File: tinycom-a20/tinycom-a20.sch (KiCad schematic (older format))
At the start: 38 parts, among them P1 CONN_02X08, P2 CONN_02X08, U1 ALLWINNERA10/TFBGA441, U2 H5TQG63BFR/FBGA96, U3 H27UBG8T2A/TSOP48, U4 H5TQG63BFR/FBGA96, Y1 Crystal_Small, Y2 Crystal_Small

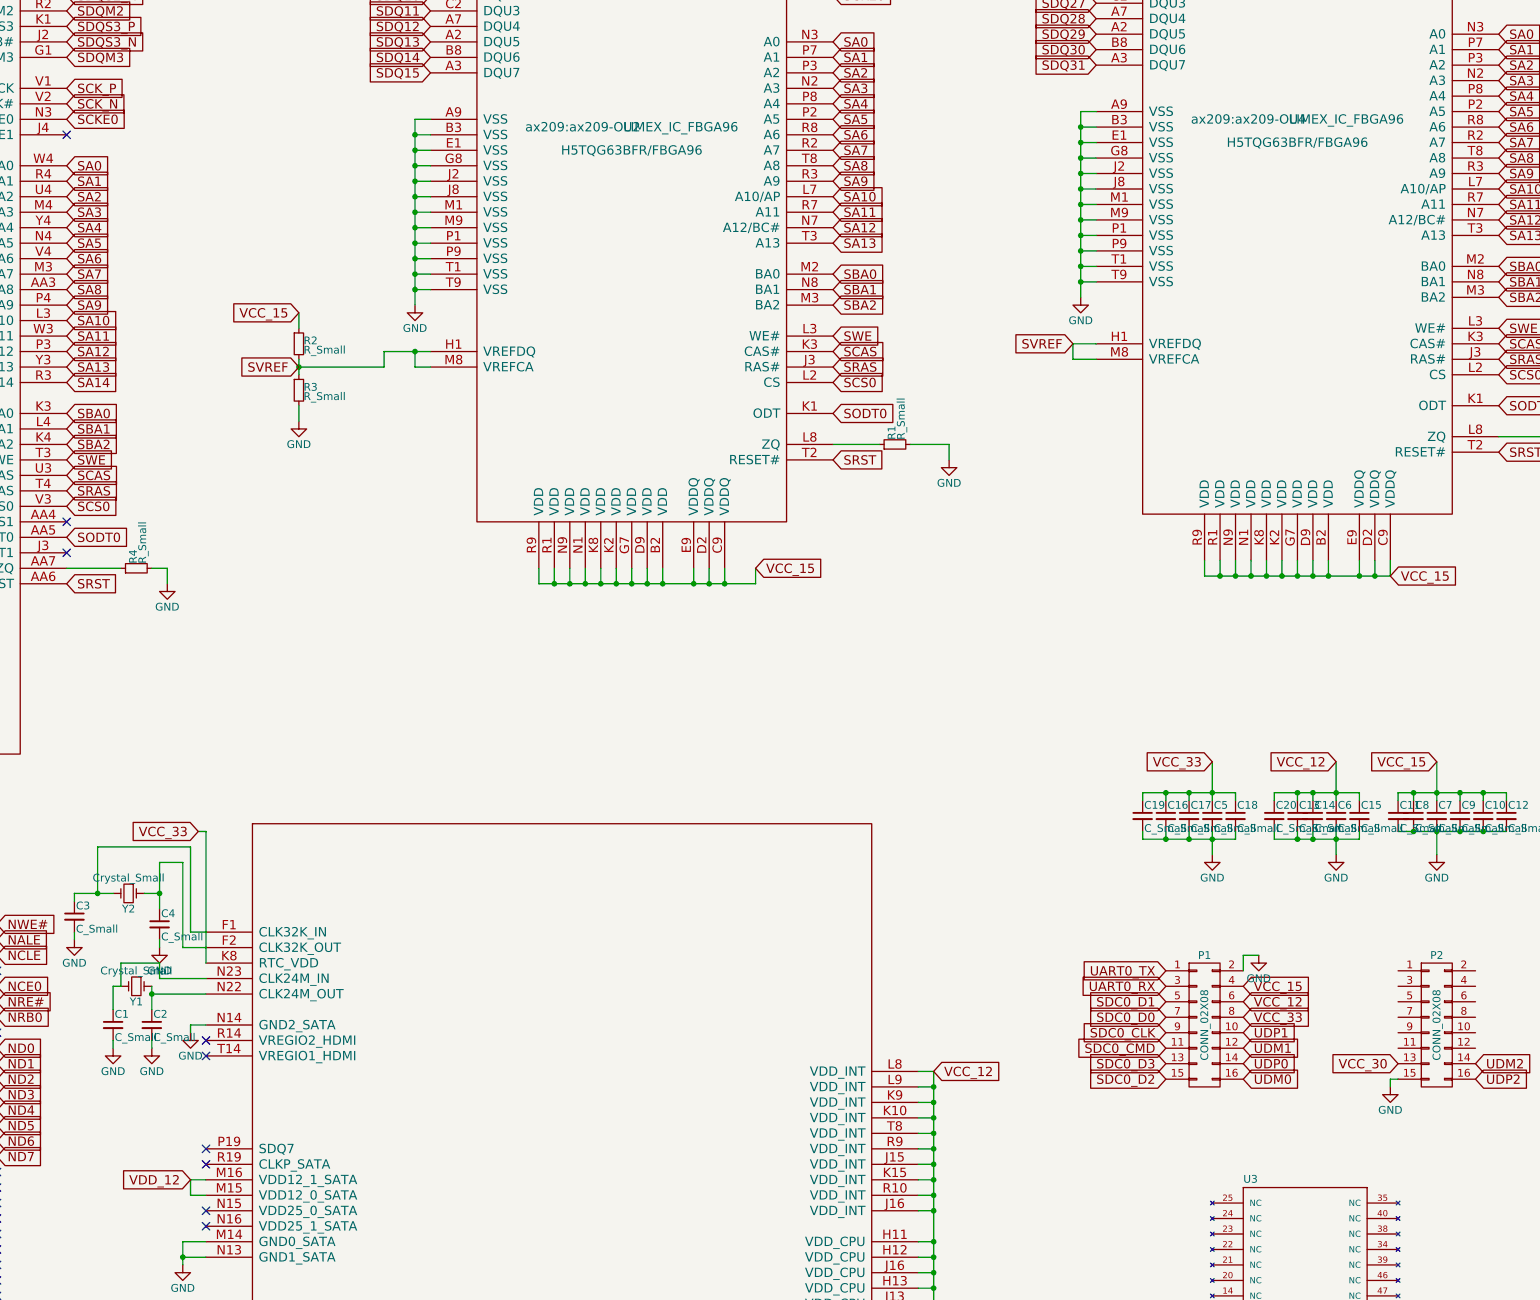
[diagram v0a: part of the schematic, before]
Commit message: change track/via size settings, update ddr footprints
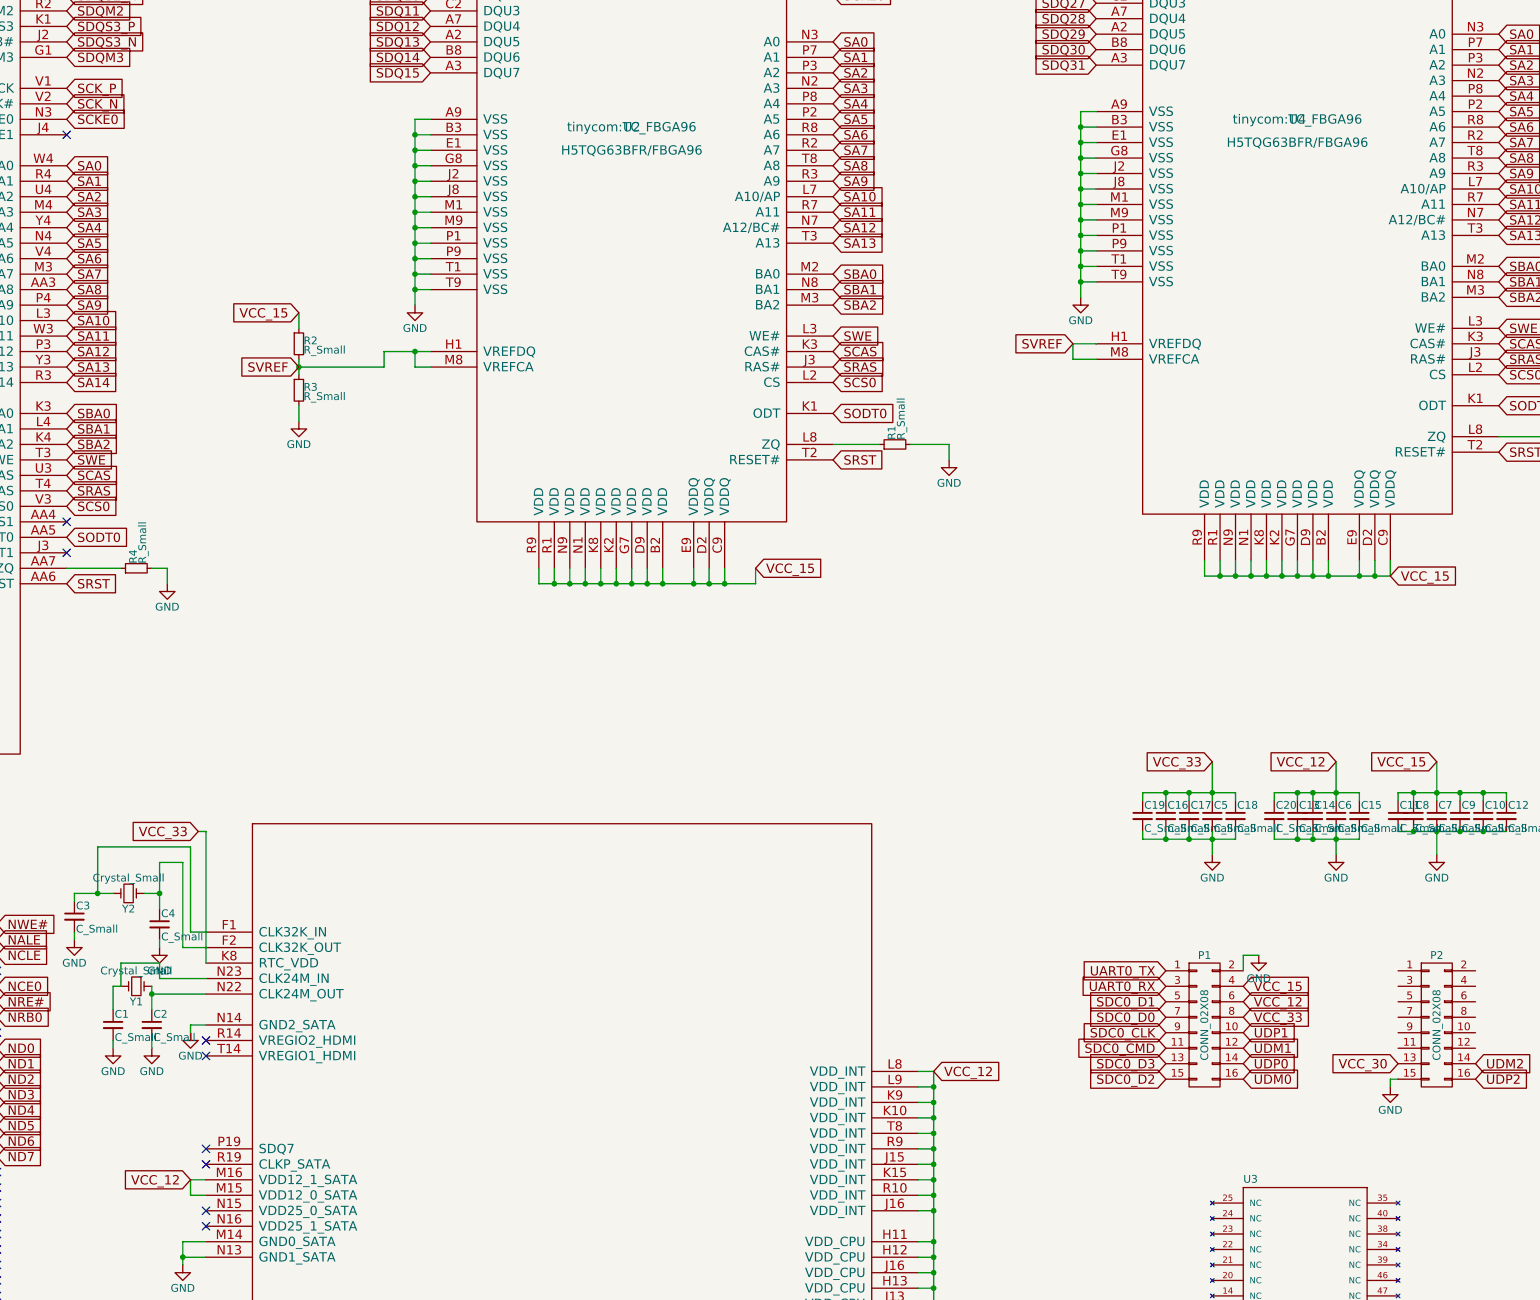
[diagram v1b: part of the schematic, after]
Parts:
- U2, U4: footprint ax209:ax209-OLIMEX_IC_FBGA96 -> tinycom:TC_FBGA96
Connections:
- net VDD_12 is gone; now on net VCC_12: U1.M15 (VDD12_0_SATA), U1.M16 (VDD12_1_SATA)
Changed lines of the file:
@@
 $EndComp
 $Comp
-L GND #PWR21
+L GND #PWR01
 U 1 1 563E445F
 P 17800 6150
-F 0 "#PWR21" H 17800 5900 50  0001 C CNN
+F 0 "#PWR01" H 17800 5900 50  0001 C CNN
 F 1 "GND" H 17800 6000 50  0000 C CNN
 F 2 "" H 17800 6150 60  0000 C CNN
@@
 F 0 "U2" H 15750 4000 60  0000 C CNN
 F 1 "H5TQG63BFR/FBGA96" H 15750 3850 60  0000 C CNN
-F 2 "ax209:ax209-OLIMEX_IC_FBGA96" H 15750 4000 60  0000 C CNN
+F 2 "tinycom:TC_FBGA96" H 15750 4000 60  0000 C CNN
 F 3 "" H 15750 4000 60  0000 C CNN
 	1    15750 4000
@@
 SCK_P
 $Comp
-L GND #PWR19
+L GND #PWR02
 U 1 1 563ECE56
 P 14950 850
-F 0 "#PWR19" H 14950 600 50  0001 C CNN
+F 0 "#PWR02" H 14950 600 50  0001 C CNN
 F 1 "GND" H 14950 700 50  0000 C CNN
 F 2 "" H 14950 850 60  0000 C CNN
@@
 $EndComp
 $Comp
-L GND #PWR17
+L GND #PWR03
 U 1 1 563EDF36
 P 13600 5900
-F 0 "#PWR17" H 13600 5650 50  0001 C CNN
+F 0 "#PWR03" H 13600 5650 50  0001 C CNN
 F 1 "GND" H 13600 5750 50  0000 C CNN
 F 2 "" H 13600 5900 60  0000 C CNN
@@
 $EndComp
 $Comp
-L GND #PWR18
+L GND #PWR04
 U 1 1 563EE398
 P 14350 5150
-F 0 "#PWR18" H 14350 4900 50  0001 C CNN
+F 0 "#PWR04" H 14350 4900 50  0001 C CNN
 F 1 "GND" H 14350 5000 50  0000 C CNN
 F 2 "" H 14350 5150 60  0000 C CNN
@@
 $EndComp
 $Comp
-L GND #PWR10
+L GND #PWR05
 U 1 1 56400687
 P 12400 9950
-F 0 "#PWR10" H 12400 9700 50  0001 C CNN
+F 0 "#PWR05" H 12400 9700 50  0001 C CNN
 F 1 "GND" H 12400 9800 50  0000 C CNN
 F 2 "" H 12400 9950 60  0000 C CNN
@@
 $EndComp
 $Comp
-L GND #PWR11
+L GND #PWR06
 U 1 1 56400704
 P 12650 9950
-F 0 "#PWR11" H 12650 9700 50  0001 C CNN
+F 0 "#PWR06" H 12650 9700 50  0001 C CNN
 F 1 "GND" H 12650 9800 50  0000 C CNN
 F 2 "" H 12650 9950 60  0000 C CNN
@@
 $EndComp
 $Comp
-L GND #PWR9
+L GND #PWR07
 U 1 1 56408532
 P 12150 9250
-F 0 "#PWR9" H 12150 9000 50  0001 C CNN
+F 0 "#PWR07" H 12150 9000 50  0001 C CNN
 F 1 "GND" H 12150 9100 50  0000 C CNN
 F 2 "" H 12150 9250 60  0000 C CNN
@@
 $EndComp
 $Comp
-L GND #PWR12
+L GND #PWR08
 U 1 1 56408573
 P 12700 9300
-F 0 "#PWR12" H 12700 9050 50  0001 C CNN
+F 0 "#PWR08" H 12700 9050 50  0001 C CNN
 F 1 "GND" H 12700 9150 50  0000 C CNN
 F 2 "" H 12700 9300 60  0000 C CNN
@@
 $EndComp
 $Comp
-L GND #PWR14
+L GND #PWR09
 U 1 1 5640D8CA
 P 12750 6950
-F 0 "#PWR14" H 12750 6700 50  0001 C CNN
+F 0 "#PWR09" H 12750 6700 50  0001 C CNN
 F 1 "GND" H 12750 6800 50  0000 C CNN
 F 2 "" H 12750 6950 60  0000 C CNN
@@
 $EndComp
 $Comp
-L GND #PWR26
+L GND #PWR010
 U 1 1 56408FCA
 P 19800 9350
-F 0 "#PWR26" H 19800 9100 50  0001 C CNN
+F 0 "#PWR010" H 19800 9100 50  0001 C CNN
 F 1 "GND" H 19800 9200 50  0000 C CNN
 F 2 "" H 19800 9350 60  0000 C CNN
@@
 UDP2
 $Comp
-L GND #PWR28
+L GND #PWR011
 U 1 1 56411561
 P 20650 10200
-F 0 "#PWR28" H 20650 9950 50  0001 C CNN
+F 0 "#PWR011" H 20650 9950 50  0001 C CNN
 F 1 "GND" H 20650 10050 50  0000 C CNN
 F 2 "" H 20650 10200 60  0000 C CNN
@@
 NoConn ~ 7500 2750
 $Comp
-L GND #PWR8
+L GND #PWR012
 U 1 1 56414A5D
 P 8850 1300
-F 0 "#PWR8" H 8850 1050 50  0001 C CNN
+F 0 "#PWR012" H 8850 1050 50  0001 C CNN
 F 1 "GND" H 8850 1150 50  0000 C CNN
 F 2 "" H 8850 1300 60  0000 C CNN
@@
 VCC_15
 $Comp
-L GND #PWR1
+L GND #PWR013
 U 1 1 56417328
 P 800 9350
-F 0 "#PWR1" H 800 9100 50  0001 C CNN
+F 0 "#PWR013" H 800 9100 50  0001 C CNN
 F 1 "GND" H 800 9200 50  0000 C CNN
 F 2 "" H 800 9350 60  0000 C CNN
@@
 NoConn ~ 1050 13300
 $Comp
-L GND #PWR3
+L GND #PWR014
 U 1 1 56417B02
 P 900 13450
-F 0 "#PWR3" H 900 13200 50  0001 C CNN
+F 0 "#PWR014" H 900 13200 50  0001 C CNN
 F 1 "GND" H 900 13300 50  0000 C CNN
 F 2 "" H 900 13450 60  0000 C CNN
@@
 NoConn ~ 1050 13700
 $Comp
-L GND #PWR2
+L GND #PWR015
 U 1 1 56417F5A
 P 850 13800
-F 0 "#PWR2" H 850 13550 50  0001 C CNN
+F 0 "#PWR015" H 850 13550 50  0001 C CNN
 F 1 "GND" H 850 13650 50  0000 C CNN
 F 2 "" H 850 13800 60  0000 C CNN
@@
 NoConn ~ 5650 11400
 $Comp
-L GND #PWR6
+L GND #PWR016
 U 1 1 56418E41
 P 5850 12050
-F 0 "#PWR6" H 5850 11800 50  0001 C CNN
+F 0 "#PWR016" H 5850 11800 50  0001 C CNN
 F 1 "GND" H 5850 11900 50  0000 C CNN
 F 2 "" H 5850 12050 60  0000 C CNN
@@
 $EndComp
 $Comp
-L GND #PWR7
+L GND #PWR017
 U 1 1 56419222
 P 5900 12300
-F 0 "#PWR7" H 5900 12050 50  0001 C CNN
+F 0 "#PWR017" H 5900 12050 50  0001 C CNN
 F 1 "GND" H 5900 12150 50  0000 C CNN
 F 2 "" H 5900 12300 60  0000 C CNN
@@
 NoConn ~ 11650 14450
 $Comp
-L GND #PWR16
+L GND #PWR018
 U 1 1 5641B53D
 P 12900 9850
-F 0 "#PWR16" H 12900 9600 50  0001 C CNN
+F 0 "#PWR018" H 12900 9600 50  0001 C CNN
 F 1 "GND" H 12900 9700 50  0000 C CNN
 F 2 "" H 12900 9850 60  0000 C CNN
@@
 NoConn ~ 13000 10700
 $Comp
-L GND #PWR15
+L GND #PWR019
 U 1 1 5641BA06
 P 12850 11350
-F 0 "#PWR15" H 12850 11100 50  0001 C CNN
+F 0 "#PWR019" H 12850 11100 50  0001 C CNN
 F 1 "GND" H 12850 11200 50  0000 C CNN
 F 2 "" H 12850 11350 60  0000 C CNN
@@
 NoConn ~ 13000 12600
 $Comp
-L GND #PWR13
+L GND #PWR020
 U 1 1 5641C0BF
 P 12700 12700
-F 0 "#PWR13" H 12700 12450 50  0001 C CNN
+F 0 "#PWR020" H 12700 12450 50  0001 C CNN
 F 1 "GND" H 12700 12550 50  0000 C CNN
 F 2 "" H 12700 12700 60  0000 C CNN
@@
 $EndComp
 $Comp
-L GND #PWR20
+L GND #PWR021
 U 1 1 5641C64B
 P 17750 14500
-F 0 "#PWR20" H 17750 14250 50  0001 C CNN
+F 0 "#PWR021" H 17750 14250 50  0001 C CNN
 F 1 "GND" H 17750 14350 50  0000 C CNN
 F 2 "" H 17750 14500 60  0000 C CNN
@@
 $EndComp
 $Comp
-L GND #PWR22
+L GND #PWR022
 U 1 1 5641CC6D
 P 17800 13850
-F 0 "#PWR22" H 17800 13600 50  0001 C CNN
+F 0 "#PWR022" H 17800 13600 50  0001 C CNN
 F 1 "GND" H 17800 13700 50  0000 C CNN
 F 2 "" H 17800 13850 60  0000 C CNN
@@
 VCC_33
 Text GLabel 12900 10800 0    60   Input ~ 0
-VDD_12
+VCC_12
 Text GLabel 12900 13250 0    60   Input ~ 0
 VCC_33
@@
 VCC_33
 $Comp
-L GND #PWR29
+L GND #PWR023
 U 1 1 5643044F
 P 20800 13600
-F 0 "#PWR29" H 20800 13350 50  0001 C CNN
+F 0 "#PWR023" H 20800 13350 50  0001 C CNN
 F 1 "GND" H 20800 13450 50  0000 C CNN
 F 2 "" H 20800 13600 60  0000 C CNN
@@
 VCC_33
 $Comp
-L GND #PWR5
+L GND #PWR024
 U 1 1 5643A4FE
 P 5850 10900
-F 0 "#PWR5" H 5850 10650 50  0001 C CNN
+F 0 "#PWR024" H 5850 10650 50  0001 C CNN
 F 1 "GND" H 5850 10750 50  0000 C CNN
 F 2 "" H 5850 10900 60  0000 C CNN
@@
 NoConn ~ 1050 14100
 $Comp
-L GND #PWR4
+L GND #PWR025
 U 1 1 5643BDD7
 P 950 11000
-F 0 "#PWR4" H 950 10750 50  0001 C CNN
+F 0 "#PWR025" H 950 10750 50  0001 C CNN
 F 1 "GND" H 950 10850 50  0000 C CNN
 F 2 "" H 950 11000 60  0000 C CNN
@@
 VCC_33
 $Comp
-L GND #PWR25
+L GND #PWR026
 U 1 1 56440C85
 P 19500 8700
-F 0 "#PWR25" H 19500 8450 50  0001 C CNN
+F 0 "#PWR026" H 19500 8450 50  0001 C CNN
 F 1 "GND" H 19500 8550 50  0000 C CNN
 F 2 "" H 19500 8700 60  0000 C CNN
@@
 $EndComp
 $Comp
-L GND #PWR27
+L GND #PWR027
 U 1 1 56441E51
 P 20300 8700
-F 0 "#PWR27" H 20300 8450 50  0001 C CNN
+F 0 "#PWR027" H 20300 8450 50  0001 C CNN
 F 1 "GND" H 20300 8550 50  0000 C CNN
 F 2 "" H 20300 8700 60  0000 C CNN
@@
 $EndComp
 $Comp
-L GND #PWR30
+L GND #PWR028
 U 1 1 564426D1
 P 20950 8700
-F 0 "#PWR30" H 20950 8450 50  0001 C CNN
+F 0 "#PWR028" H 20950 8450 50  0001 C CNN
 F 1 "GND" H 20950 8550 50  0000 C CNN
 F 2 "" H 20950 8700 60  0000 C CNN
@@
 F 0 "U4" H 20050 3950 60  0000 C CNN
 F 1 "H5TQG63BFR/FBGA96" H 20050 3800 60  0000 C CNN
-F 2 "ax209:ax209-OLIMEX_IC_FBGA96" H 20050 3950 60  0000 C CNN
+F 2 "tinycom:TC_FBGA96" H 20050 3950 60  0000 C CNN
 F 3 "" H 20050 3950 60  0000 C CNN
 	1    20050 3950
@@
 VCC_15
 $Comp
-L GND #PWR24
+L GND #PWR029
 U 1 1 564464B9
 P 19300 750
-F 0 "#PWR24" H 19300 500 50  0001 C CNN
+F 0 "#PWR029" H 19300 500 50  0001 C CNN
 F 1 "GND" H 19300 600 50  0000 C CNN
 F 2 "" H 19300 750 60  0000 C CNN
@@
 $EndComp
 $Comp
-L GND #PWR31
+L GND #PWR030
 U 1 1 56448F6B
 P 22100 6100
-F 0 "#PWR31" H 22100 5850 50  0001 C CNN
+F 0 "#PWR030" H 22100 5850 50  0001 C CNN
 F 1 "GND" H 22100 5950 50  0000 C CNN
 F 2 "" H 22100 6100 60  0000 C CNN
@@
 Connection ~ 18650 4900
 $Comp
-L GND #PWR23
+L GND #PWR031
 U 1 1 5644D663
 P 18650 5100
-F 0 "#PWR23" H 18650 4850 50  0001 C CNN
+F 0 "#PWR031" H 18650 4850 50  0001 C CNN
 F 1 "GND" H 18650 4950 50  0000 C CNN
 F 2 "" H 18650 5100 60  0000 C CNN

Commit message: before import routes
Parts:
- removed R10: R_Small, Resistors_SMD:R_0603, symbol R_Small
- removed U4: H5TQG63BFR/FBGA96, tinycom:TC_FBGA96, symbol H5TQG63BFR/FBGA96
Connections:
- no-connect marks 239 -> 233

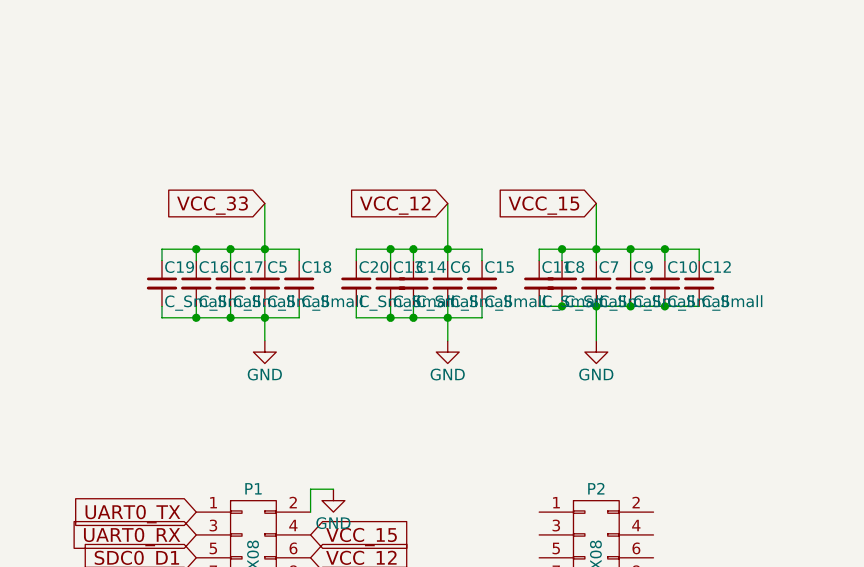
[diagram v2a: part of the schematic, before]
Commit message: add power/gnd vias
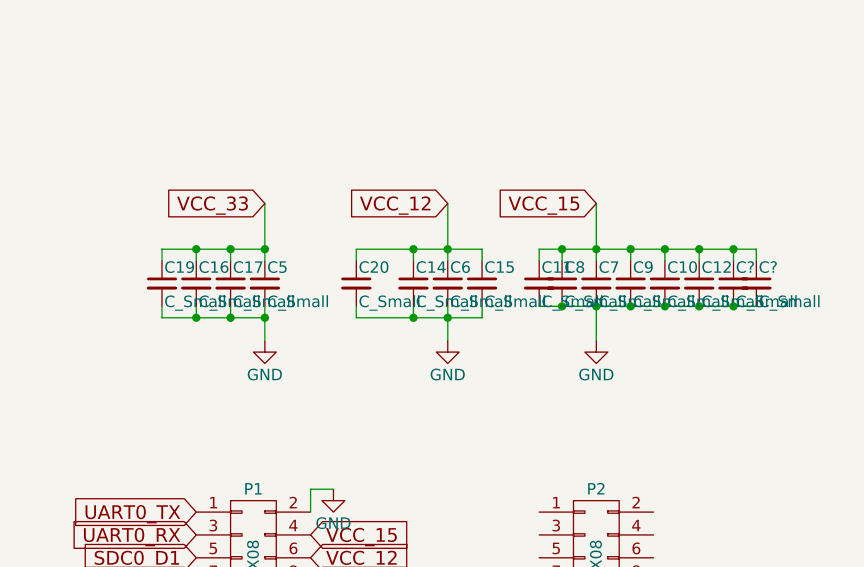
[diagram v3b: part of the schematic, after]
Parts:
- removed C13, C18: C_Small, Capacitors_SMD:C_0603, symbol C_Small
- added C? (x2): C_Small, Capacitors_SMD:C_0603, symbol C_Small
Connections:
- net GND: now also C?.2, C?.2
- net VCC_15: now also C?.1, C?.1
